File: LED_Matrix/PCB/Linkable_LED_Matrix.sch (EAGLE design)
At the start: 8 parts, among them U1 ATTINY48, U2 ULN2803AFWG

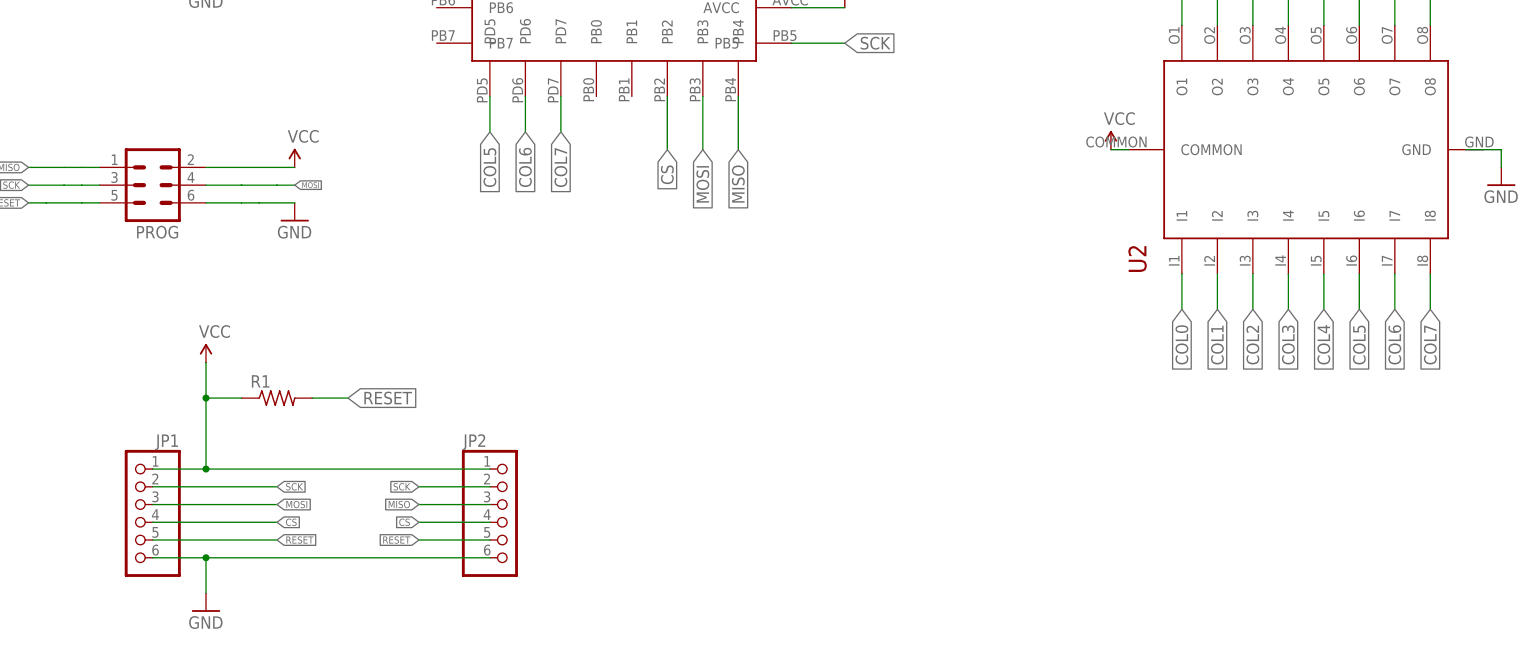
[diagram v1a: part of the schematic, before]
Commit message: cleanup to pass error checks
Stop mask fails checks for silkscreen written on top of copper, but OshPark
automatically trims that so I've approved it all.  It would be a pain to trim
it all, so I won't (unless we need to later).
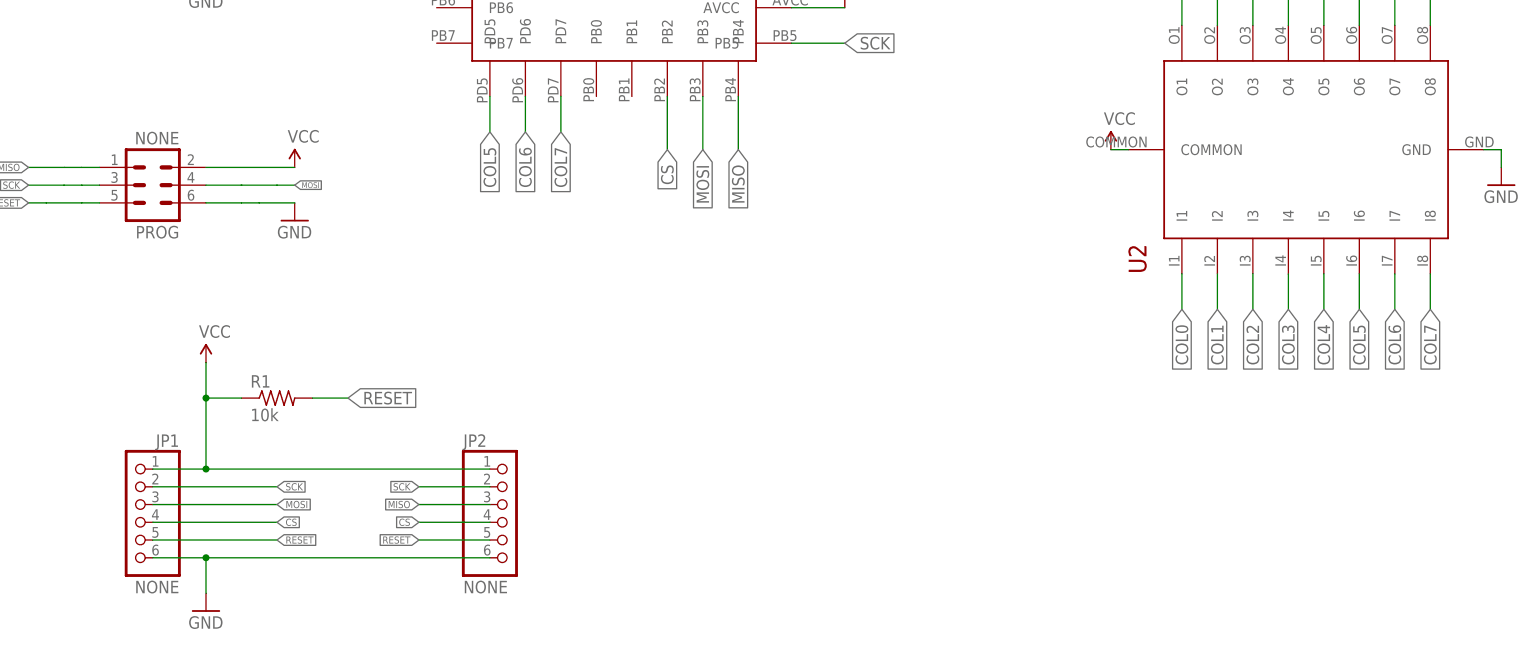
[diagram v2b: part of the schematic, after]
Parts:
- JP1, JP2, PROG: value (none) -> NONE
- R1: value (none) -> 10k
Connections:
- net GND: now also U2.GND
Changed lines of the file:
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@@
 <grid distance="0.1" unitdist="inch" unit="inch" style="lines" multiple="1" display="yes" altdistance="0.01" altunitdist="inch" altunit="inch"/>
 <layers>
-<layer number="1" name="Top" color="4" fill="1" visible="yes" active="no"/>
-<layer number="2" name="Route2" color="1" fill="3" visible="yes" active="no"/>
-<layer number="3" name="Route3" color="4" fill="3" visible="yes" active="no"/>
-<layer number="14" name="Route14" color="1" fill="6" visible="yes" active="no"/>
-<layer number="15" name="Route15" color="4" fill="6" visible="yes" active="no"/>
-<layer number="16" name="Bottom" color="1" fill="1" visible="yes" active="no"/>
-<layer number="17" name="Pads" color="2" fill="1" visible="yes" active="no"/>
-<layer number="18" name="Vias" color="2" fill="1" visible="yes" active="no"/>
-<layer number="19" name="Unrouted" color="6" fill="1" visible="yes" active="no"/>
-<layer number="20" name="Dimension" color="15" fill="1" visible="yes" active="no"/>
-<layer number="21" name="tPlace" color="7" fill="1" visible="yes" active="no"/>
-<layer number="22" name="bPlace" color="7" fill="1" visible="yes" active="no"/>
-<layer number="23" name="tOrigins" color="15" fill="1" visible="yes" active="no"/>
-<layer number="24" name="bOrigins" color="15" fill="1" visible="yes" active="no"/>
-<layer number="25" name="tNames" color="7" fill="1" visible="yes" active="no"/>
-<layer number="26" name="bNames" color="7" fill="1" visible="yes" active="no"/>
-<layer number="27" name="tValues" color="7" fill="1" visible="yes" active="no"/>
-<layer number="28" name="bValues" color="7" fill="1" visible="yes" active="no"/>
+<layer number="1" name="Top" color="4" fill="1" visible="no" active="no"/>
+<layer number="2" name="Route2" color="1" fill="3" visible="no" active="no"/>
+<layer number="3" name="Route3" color="4" fill="3" visible="no" active="no"/>
+<layer number="14" name="Route14" color="1" fill="6" visible="no" active="no"/>
+<layer number="15" name="Route15" color="4" fill="6" visible="no" active="no"/>
+<layer number="16" name="Bottom" color="1" fill="1" visible="no" active="no"/>
+<layer number="17" name="Pads" color="2" fill="1" visible="no" active="no"/>
+<layer number="18" name="Vias" color="2" fill="1" visible="no" active="no"/>
+<layer number="19" name="Unrouted" color="6" fill="1" visible="no" active="no"/>
+<layer number="20" name="Dimension" color="15" fill="1" visible="no" active="no"/>
+<layer number="21" name="tPlace" color="7" fill="1" visible="no" active="no"/>
+<layer number="22" name="bPlace" color="7" fill="1" visible="no" active="no"/>
+<layer number="23" name="tOrigins" color="15" fill="1" visible="no" active="no"/>
+<layer number="24" name="bOrigins" color="15" fill="1" visible="no" active="no"/>
+<layer number="25" name="tNames" color="7" fill="1" visible="no" active="no"/>
+<layer number="26" name="bNames" color="7" fill="1" visible="no" active="no"/>
+<layer number="27" name="tValues" color="7" fill="1" visible="no" active="no"/>
+<layer number="28" name="bValues" color="7" fill="1" visible="no" active="no"/>
 <layer number="29" name="tStop" color="7" fill="3" visible="no" active="no"/>
 <layer number="30" name="bStop" color="7" fill="6" visible="no" active="no"/>
@@
 <layer number="35" name="tGlue" color="7" fill="4" visible="no" active="no"/>
 <layer number="36" name="bGlue" color="7" fill="5" visible="no" active="no"/>
-<layer number="37" name="tTest" color="7" fill="1" visible="yes" active="no"/>
-<layer number="38" name="bTest" color="7" fill="1" visible="yes" active="no"/>
+<layer number="37" name="tTest" color="7" fill="1" visible="no" active="no"/>
+<layer number="38" name="bTest" color="7" fill="1" visible="no" active="no"/>
 <layer number="39" name="tKeepout" color="4" fill="11" visible="no" active="no"/>
 <layer number="40" name="bKeepout" color="1" fill="11" visible="no" active="no"/>
@@
 <layer number="44" name="Drills" color="7" fill="1" visible="no" active="no"/>
 <layer number="45" name="Holes" color="7" fill="1" visible="no" active="no"/>
-<layer number="46" name="Milling" color="3" fill="1" visible="yes" active="no"/>
-<layer number="47" name="Measures" color="7" fill="1" visible="yes" active="no"/>
-<layer number="48" name="Document" color="7" fill="1" visible="yes" active="no"/>
-<layer number="49" name="Reference" color="7" fill="1" visible="yes" active="no"/>
-<layer number="50" name="dxf" color="7" fill="1" visible="yes" active="no"/>
-<layer number="51" name="tDocu" color="7" fill="1" visible="yes" active="no"/>
-<layer number="52" name="bDocu" color="7" fill="1" visible="yes" active="no"/>
-<layer number="53" name="tGND_GNDA" color="7" fill="9" visible="yes" active="no"/>
-<layer number="54" name="bGND_GNDA" color="1" fill="9" visible="yes" active="no"/>
-<layer number="56" name="wert" color="7" fill="1" visible="yes" active="no"/>
-<layer number="57" name="tCAD" color="7" fill="1" visible="yes" active="no"/>
+<layer number="46" name="Milling" color="3" fill="1" visible="no" active="no"/>
+<layer number="47" name="Measures" color="7" fill="1" visible="no" active="no"/>
+<layer number="48" name="Document" color="7" fill="1" visible="no" active="no"/>
+<layer number="49" name="Reference" color="7" fill="1" visible="no" active="no"/>
+<layer number="50" name="dxf" color="7" fill="1" visible="no" active="no"/>
+<layer number="51" name="tDocu" color="7" fill="1" visible="no" active="no"/>
+<layer number="52" name="bDocu" color="7" fill="1" visible="no" active="no"/>
+<layer number="53" name="tGND_GNDA" color="7" fill="9" visible="no" active="no"/>
+<layer number="54" name="bGND_GNDA" color="1" fill="9" visible="no" active="no"/>
+<layer number="56" name="wert" color="7" fill="1" visible="no" active="no"/>
+<layer number="57" name="tCAD" color="7" fill="1" visible="no" active="no"/>
 <layer number="91" name="Nets" color="2" fill="1" visible="yes" active="yes"/>
 <layer number="92" name="Busses" color="1" fill="1" visible="yes" active="yes"/>
@@
 <part name="GND6" library="SparkFun-Aesthetics" deviceset="GND" device=""/>
 <part name="SUPPLY6" library="SparkFun-Aesthetics" deviceset="VCC" device=""/>
-<part name="R1" library="resistor" deviceset="R-US_" device="R0603"/>
+<part name="R1" library="resistor" deviceset="R-US_" device="R0603" value="10k"/>
 <part name="C1" library="resistor" deviceset="C-US" device="C0603" value="1uF"/>
 <part name="SUPPLY7" library="SparkFun-Aesthetics" deviceset="VCC" device=""/>
@@
 <part name="GND3" library="SparkFun-Aesthetics" deviceset="GND" device=""/>
 <part name="FRAME1" library="frames" deviceset="LETTER_L" device=""/>
-<part name="PROG" library="raspberrystem" deviceset="MA03-2" device=""/>
-<part name="JP1" library="raspberrystem" deviceset="PINHD-1X6" device=""/>
-<part name="JP2" library="raspberrystem" deviceset="PINHD-1X6" device=""/>
+<part name="PROG" library="raspberrystem" deviceset="MA03-2" device="" value="NONE"/>
+<part name="JP1" library="raspberrystem" deviceset="PINHD-1X6" device="" value="NONE"/>
+<part name="JP2" library="raspberrystem" deviceset="PINHD-1X6" device="" value="NONE"/>
 </parts>
 <sheets>
@@
 <segment>
 <pinref part="GND3" gate="1" pin="GND"/>
-<wire x1="144.78" y1="187.96" x2="149.86" y2="187.96" width="0.1524" layer="91"/>
 <wire x1="149.86" y1="187.96" x2="149.86" y2="185.42" width="0.1524" layer="91"/>
+<pinref part="U2" gate="G$1" pin="GND"/>
+<wire x1="149.86" y1="187.96" x2="147.32" y2="187.96" width="0.1524" layer="91"/>
 </segment>
 </net>
@@
 </sheet>
 </sheets>
+<errors>
+</errors>
 </schematic>
 </drawing>
